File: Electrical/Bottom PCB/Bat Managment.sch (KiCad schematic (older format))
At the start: 6 parts

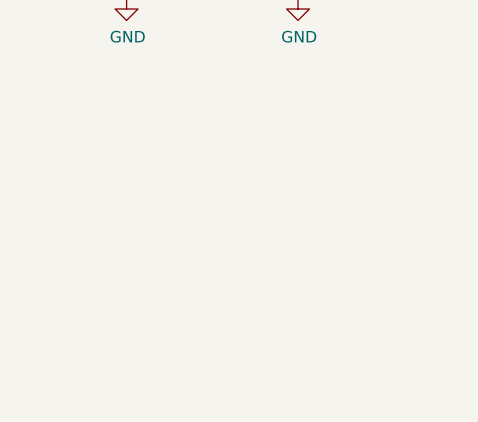
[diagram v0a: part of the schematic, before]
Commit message: removed the servos at the moment
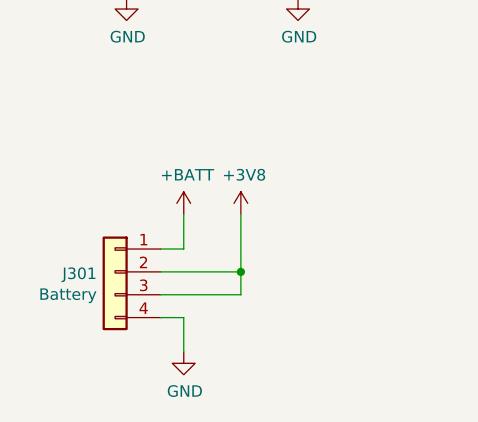
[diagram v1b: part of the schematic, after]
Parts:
- added J301: Battery, Connector_JST:JST_XH_B4B-XH-A_1x04_P2.50mm_Vertical, symbol Connector_Generic:Conn_01x04
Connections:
- net +3V8: now also J301.2 (Pin_2), J301.3 (Pin_3)
- net +BATT: now also J301.1 (Pin_1)
- net GND: now also J301.4 (Pin_4)
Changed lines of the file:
@@
 $Descr A4 11693 8268
 encoding utf-8
-Sheet 3 3
+Sheet 3 4
 Title ""
 Date ""
@@
 	1    0    0    -1
 $EndComp
+$Comp
+L Connector_Generic:Conn_01x04 J?
+U 1 1 5EBBDBE9
+P 1750 4400
+AR Path="/5EBBDBE9" Ref="J?"  Part="1"
+AR Path="/5ED67F7E/5EBBDBE9" Ref="J301"  Part="1"
+F 0 "J301" H 1830 4392 50  0000 L CNN
+F 1 "Battery" H 1830 4301 50  0000 L CNN
+F 2 "Connector_JST:JST_XH_B4B-XH-A_1x04_P2.50mm_Vertical" H 1750 4400 50  0001 C CNN
+F 3 "~" H 1750 4400 50  0001 C CNN
+	1    1750 4400
+	-1   0    0    -1
+$EndComp
+$Comp
+L power:+3V8 #PWR?
+U 1 1 5EBC1737
+P 2300 4150
+AR Path="/5EBB31C5/5EBC1737" Ref="#PWR?"  Part="1"
+AR Path="/5ED67F7E/5EBC1737" Ref="#PWR0308"  Part="1"
+F 0 "#PWR0308" H 2300 4000 50  0001 C CNN
+F 1 "+3V8" H 2315 4323 50  0000 C CNN
+F 2 "" H 2300 4150 50  0001 C CNN
+F 3 "" H 2300 4150 50  0001 C CNN
+	1    2300 4150
+	1    0    0    -1
+$EndComp
+$Comp
+L power:+BATT #PWR?
+U 1 1 5EBC1DA3
+P 2050 4150
+AR Path="/5EBC1DA3" Ref="#PWR?"  Part="1"
+AR Path="/5ED67F7E/5EBC1DA3" Ref="#PWR0307"  Part="1"
+F 0 "#PWR0307" H 2050 4000 50  0001 C CNN
+F 1 "+BATT" H 2065 4323 50  0000 C CNN
+F 2 "" H 2050 4150 50  0001 C CNN
+F 3 "" H 2050 4150 50  0001 C CNN
+	1    2050 4150
+	1    0    0    -1
+$EndComp
+$Comp
+L power:GND #PWR?
+U 1 1 5EBC24CC
+P 2050 4750
+AR Path="/5EBC24CC" Ref="#PWR?"  Part="1"
+AR Path="/5ED67F7E/5EBC24CC" Ref="#PWR0309"  Part="1"
+F 0 "#PWR0309" H 2050 4500 50  0001 C CNN
+F 1 "GND" H 2055 4577 50  0000 C CNN
+F 2 "" H 2050 4750 50  0001 C CNN
+F 3 "" H 2050 4750 50  0001 C CNN
+	1    2050 4750
+	1    0    0    -1
+$EndComp
+Wire Wire Line
+	2050 4150 2050 4300
+Wire Wire Line
+	2050 4300 1950 4300
+Wire Wire Line
+	1950 4400 2300 4400
+Wire Wire Line
+	1950 4500 2300 4500
+Wire Wire Line
+	2300 4150 2300 4400
+Connection ~ 2300 4400
+Wire Wire Line
+	2300 4400 2300 4500
+Wire Wire Line
+	1950 4600 2050 4600
+Wire Wire Line
+	2050 4600 2050 4750
 $EndSCHEMATC

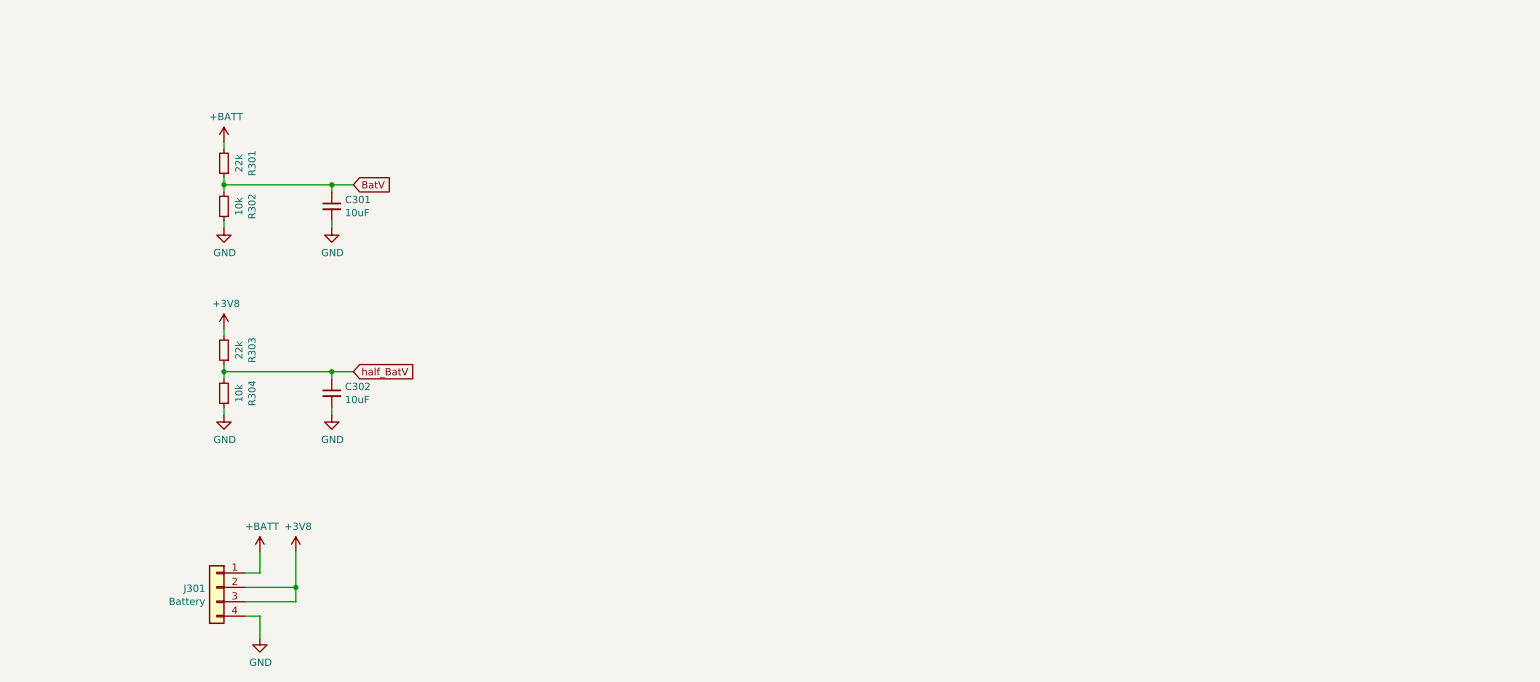
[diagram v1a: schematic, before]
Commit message: Added power switch
Some more modifications
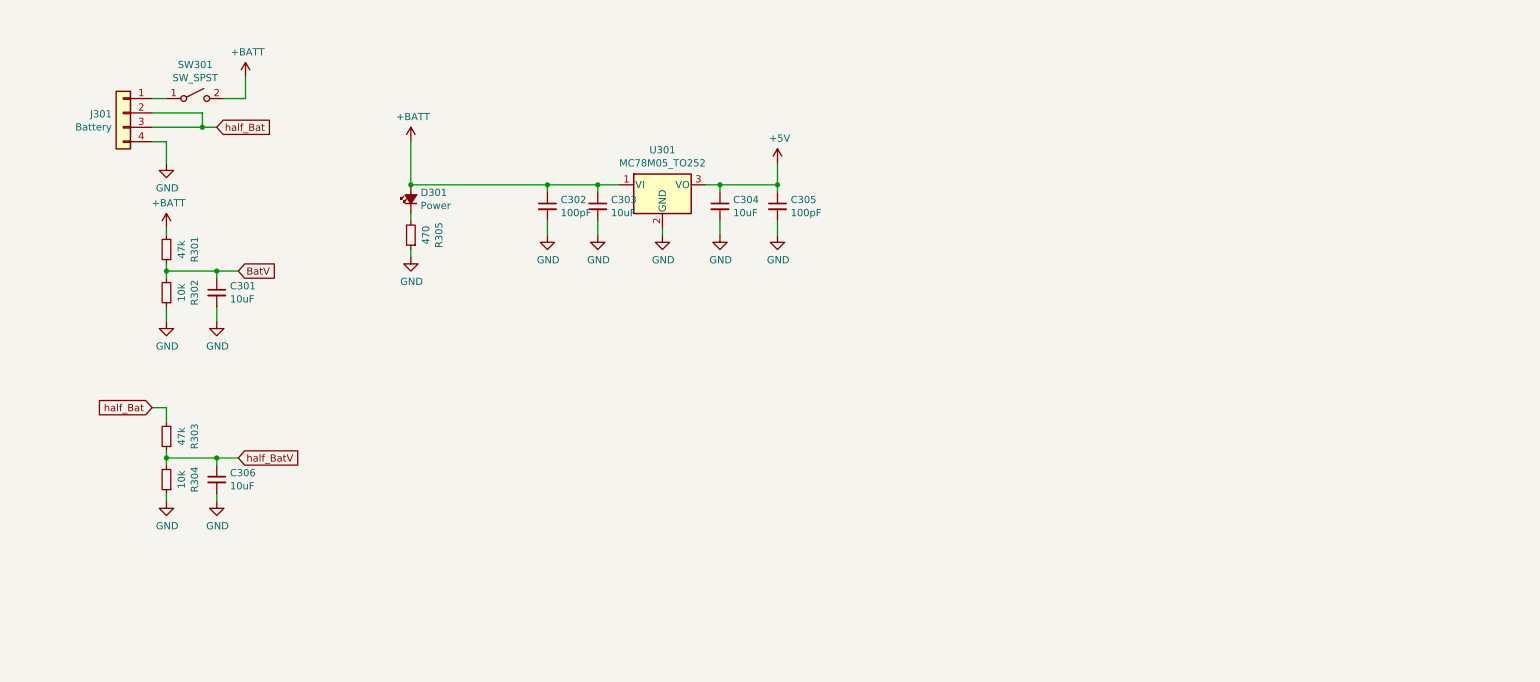
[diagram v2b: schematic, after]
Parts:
- added C302, C305: 100pF, Capacitor_SMD:C_1206_3216Metric_Pad1.42x1.75mm_HandSolder, symbol Device:C_Small
- added C303, C304: 10uF, Capacitor_SMD:C_1206_3216Metric_Pad1.42x1.75mm_HandSolder, symbol Device:C_Small
- added D301: Power, LED_SMD:LED_0805_2012Metric_Pad1.15x1.40mm_HandSolder, symbol Device:LED_Small_ALT
- added R305: 470, Resistor_SMD:R_1206_3216Metric_Pad1.42x1.75mm_HandSolder, symbol Device:R_Small
- added SW301: SW_SPST, Button_Switch_SMD:SW_SPST_B3U-3100P-B, symbol Switch:SW_SPST
- added U301: MC78M05_TO252, Package_TO_SOT_SMD:TO-252-2, symbol Regulator_Linear:MC78M05_TO252
- R301, R303: value 22k -> 47k
- renumbered C302 to C306
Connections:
- net +BATT: now also C302.1, C303.1, D301.2 (A), SW301.2 (B), U301.1 (VI); no longer J301.1 (Pin_1)
- net GND: now also C302.2, C303.2, C304.2, C305.2, R305.1, U301.2 (GND)
- net +3V8 renamed half_Bat
- new net: J301.1 (Pin_1), SW301.1 (A)
- new net: D301.1 (K), R305.2
- new net +5V: C304.1, C305.1, U301.3 (VO)
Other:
- moved on the sheet: C301, C306, J301, R301, R302, R303, R304

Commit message: added more stuff
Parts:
- renumbered C302 to C301, C303 to C302, C304 to C303, C305 to C304, C301 to C305, R303 to R302, R302 to R303
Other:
- moved on the sheet: C301, C302, C303, C304, C305, C306, D301, J301, R301, R302, R303, R304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

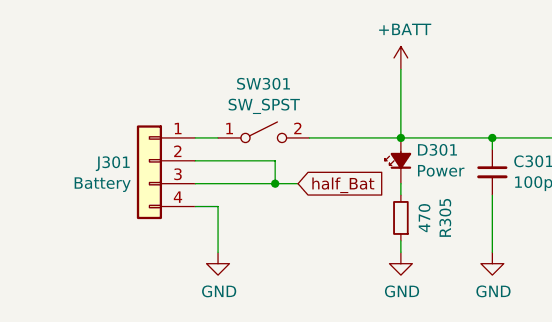
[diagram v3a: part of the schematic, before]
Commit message: changed from 1206 to 0805
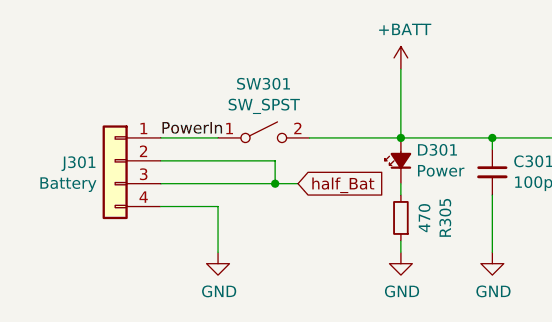
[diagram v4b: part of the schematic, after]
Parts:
- C301, C302, C303, C304, C305, C306: footprint Capacitor_SMD:C_1206_3216Metric_Pad1.42x1.75mm_HandSolder -> Capacitor_SMD:C_0805_2012Metric_Pad1.15x1.40mm_HandSolder
- R301, R302, R303, R304, R305: footprint Resistor_SMD:R_1206_3216Metric_Pad1.42x1.75mm_HandSolder -> Resistor_SMD:R_0805_2012Metric_Pad1.15x1.40mm_HandSolder
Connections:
- net PowerIn: now reaches J301.1 (Pin_1), SW301.1 (A)
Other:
- moved on the sheet: J301
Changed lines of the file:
@@
 F 0 "R303" V 5004 1100 50  0000 C CNN
 F 1 "10k" V 5095 1100 50  0000 C CNN
-F 2 "Resistor_SMD:R_1206_3216Metric_Pad1.42x1.75mm_HandSolder" H 5200 1100 50  0001 C CNN
+F 2 "Resistor_SMD:R_0805_2012Metric_Pad1.15x1.40mm_HandSolder" H 5200 1100 50  0001 C CNN
 F 3 "~" H 5200 1100 50  0001 C CNN
 	1    5200 1100
@@
 F 0 "R301" V 5004 800 50  0000 C CNN
 F 1 "47k" V 5095 800 50  0000 C CNN
-F 2 "Resistor_SMD:R_1206_3216Metric_Pad1.42x1.75mm_HandSolder" H 5200 800 50  0001 C CNN
+F 2 "Resistor_SMD:R_0805_2012Metric_Pad1.15x1.40mm_HandSolder" H 5200 800 50  0001 C CNN
 F 3 "~" H 5200 800 50  0001 C CNN
 	1    5200 800
@@
 F 0 "R304" V 6204 1100 50  0000 C CNN
 F 1 "10k" V 6295 1100 50  0000 C CNN
-F 2 "Resistor_SMD:R_1206_3216Metric_Pad1.42x1.75mm_HandSolder" H 6400 1100 50  0001 C CNN
+F 2 "Resistor_SMD:R_0805_2012Metric_Pad1.15x1.40mm_HandSolder" H 6400 1100 50  0001 C CNN
 F 3 "~" H 6400 1100 50  0001 C CNN
 	1    6400 1100
@@
 F 0 "R302" V 6204 800 50  0000 C CNN
 F 1 "47k" V 6295 800 50  0000 C CNN
-F 2 "Resistor_SMD:R_1206_3216Metric_Pad1.42x1.75mm_HandSolder" H 6400 800 50  0001 C CNN
+F 2 "Resistor_SMD:R_0805_2012Metric_Pad1.15x1.40mm_HandSolder" H 6400 800 50  0001 C CNN
 F 3 "~" H 6400 800 50  0001 C CNN
 	1    6400 800
@@
 F 0 "C306" H 6842 1146 50  0000 L CNN
 F 1 "10uF" H 6842 1055 50  0000 L CNN
-F 2 "Capacitor_SMD:C_1206_3216Metric_Pad1.42x1.75mm_HandSolder" H 6750 1100 50  0001 C CNN
+F 2 "Capacitor_SMD:C_0805_2012Metric_Pad1.15x1.40mm_HandSolder" H 6750 1100 50  0001 C CNN
 F 3 "~" H 6750 1100 50  0001 C CNN
 	1    6750 1100
@@
 L Connector_Generic:Conn_01x04 J?
 U 1 1 5EBBDBE9
-P 1400 1050
+P 1250 1050
 AR Path="/5EBBDBE9" Ref="J?"  Part="1"
 AR Path="/5ED67F7E/5EBBDBE9" Ref="J301"  Part="1"
-F 0 "J301" H 1480 1042 50  0000 L CNN
-F 1 "Battery" H 1480 951 50  0000 L CNN
-F 2 "Connector_JST:JST_XH_B4B-XH-A_1x04_P2.50mm_Vertical" H 1400 1050 50  0001 C CNN
-F 3 "~" H 1400 1050 50  0001 C CNN
-	1    1400 1050
+F 0 "J301" H 1330 1042 50  0000 L CNN
+F 1 "Battery" H 1330 951 50  0000 L CNN
+F 2 "Connector_JST:JST_XH_B4B-XH-A_1x04_P2.50mm_Vertical" H 1250 1050 50  0001 C CNN
+F 3 "~" H 1250 1050 50  0001 C CNN
+	1    1250 1050
 	-1   0    0    -1
 $EndComp
@@
 $EndComp
 Wire Wire Line
-	1600 950  1700 950
-Wire Wire Line
-	1600 1050 1950 1050
-Wire Wire Line
-	1600 1150 1950 1150
+	1450 950  1700 950
+Wire Wire Line
+	1450 1050 1950 1050
+Wire Wire Line
+	1450 1150 1950 1150
 Wire Wire Line
 	1950 1050 1950 1150
 Wire Wire Line
-	1600 1250 1700 1250
+	1450 1250 1700 1250
 Wire Wire Line
 	1700 1250 1700 1450
@@
 F 0 "C302" H 3392 1146 50  0000 L CNN
 F 1 "10uF" H 3392 1055 50  0000 L CNN
-F 2 "Capacitor_SMD:C_1206_3216Metric_Pad1.42x1.75mm_HandSolder" H 3300 1100 50  0001 C CNN
+F 2 "Capacitor_SMD:C_0805_2012Metric_Pad1.15x1.40mm_HandSolder" H 3300 1100 50  0001 C CNN
 F 3 "~" H 3300 1100 50  0001 C CNN
 	1    3300 1100
@@
 F 0 "C301" H 2992 1146 50  0000 L CNN
 F 1 "100pF" H 2992 1055 50  0000 L CNN
-F 2 "Capacitor_SMD:C_1206_3216Metric_Pad1.42x1.75mm_HandSolder" H 2900 1100 50  0001 C CNN
+F 2 "Capacitor_SMD:C_0805_2012Metric_Pad1.15x1.40mm_HandSolder" H 2900 1100 50  0001 C CNN
 F 3 "~" H 2900 1100 50  0001 C CNN
 	1    2900 1100
@@
 F 0 "C303" H 4292 1146 50  0000 L CNN
 F 1 "10uF" H 4292 1055 50  0000 L CNN
-F 2 "Capacitor_SMD:C_1206_3216Metric_Pad1.42x1.75mm_HandSolder" H 4200 1100 50  0001 C CNN
+F 2 "Capacitor_SMD:C_0805_2012Metric_Pad1.15x1.40mm_HandSolder" H 4200 1100 50  0001 C CNN
 F 3 "~" H 4200 1100 50  0001 C CNN
 	1    4200 1100
@@
 F 0 "C304" H 4692 1146 50  0000 L CNN
 F 1 "100pF" H 4692 1055 50  0000 L CNN
-F 2 "Capacitor_SMD:C_1206_3216Metric_Pad1.42x1.75mm_HandSolder" H 4600 1100 50  0001 C CNN
+F 2 "Capacitor_SMD:C_0805_2012Metric_Pad1.15x1.40mm_HandSolder" H 4600 1100 50  0001 C CNN
 F 3 "~" H 4600 1100 50  0001 C CNN
 	1    4600 1100
@@
 F 0 "C305" H 5642 1146 50  0000 L CNN
 F 1 "10uF" H 5642 1055 50  0000 L CNN
-F 2 "Capacitor_SMD:C_1206_3216Metric_Pad1.42x1.75mm_HandSolder" H 5550 1100 50  0001 C CNN
+F 2 "Capacitor_SMD:C_0805_2012Metric_Pad1.15x1.40mm_HandSolder" H 5550 1100 50  0001 C CNN
 F 3 "~" H 5550 1100 50  0001 C CNN
 	1    5550 1100
@@
 F 0 "R305" V 2304 1300 50  0000 C CNN
 F 1 "470" V 2395 1300 50  0000 C CNN
-F 2 "Resistor_SMD:R_1206_3216Metric_Pad1.42x1.75mm_HandSolder" H 2500 1300 50  0001 C CNN
+F 2 "Resistor_SMD:R_0805_2012Metric_Pad1.15x1.40mm_HandSolder" H 2500 1300 50  0001 C CNN
 F 3 "~" H 2500 1300 50  0001 C CNN
 	1    2500 1300
@@
 Wire Wire Line
 	2100 950  2500 950
+Text Label 1450 950  0    50   ~ 0
+PowerIn
 $EndSCHEMATC

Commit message: hello
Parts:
- removed C306: 10uF, Capacitor_SMD:C_0805_2012Metric_Pad1.15x1.40mm_HandSolder, symbol Device:C_Small
- removed R304: 10k, Resistor_SMD:R_0805_2012Metric_Pad1.15x1.40mm_HandSolder, symbol Device:R_Small
- removed U301: MC78M05_TO252, Package_TO_SOT_SMD:TO-252-2, symbol Regulator_Linear:MC78M05_TO252
- added C306, C308: 1uF, Capacitor_SMD:C_0603_1608Metric_Pad1.05x0.95mm_HandSolder, symbol Device:C
- added C307: 10uF, Capacitor_SMD:C_1206_3216Metric_Pad1.42x1.75mm_HandSolder, symbol Device:C
- added C309: 0.1uF, Capacitor_SMD:C_0603_1608Metric_Pad1.05x0.95mm_HandSolder, symbol Device:C
- added C310: 10uF, Capacitor_SMD:C_0805_2012Metric_Pad1.15x1.40mm_HandSolder, symbol Device:C
- added C311: 10uF, Capacitor_SMD:C_0805_2012Metric_Pad1.15x1.40mm_HandSolder, symbol Device:C_Small
- added D301, D303, D304, D307, D308, D309, D310, D311: SS24, Diode_SMD:D_SMB-SMC_Universal_Handsoldering, symbol Device:D_Schottky_Small_ALT
- added D305: Charging, LED_SMD:LED_0805_2012Metric_Pad1.15x1.40mm_HandSolder, symbol Device:LED_Small_ALT
- added D306: Standby, LED_SMD:LED_0805_2012Metric_Pad1.15x1.40mm_HandSolder, symbol Device:LED_Small_ALT
- added H301: +VE, TestPoint:TestPoint_Pad_D2.0mm, symbol Connector_Generic:Conn_01x01
- added H302: -Ve, TestPoint:TestPoint_Pad_D2.0mm, symbol Connector_Generic:Conn_01x01
- added J302: Charging Header, symbol Connector_Generic:Conn_01x02
- added L301: 3.3uH, symbol Device:L_Core_Iron_Small
- added R305: 30k, Resistor_SMD:R_0603_1608Metric_Pad0.98x0.95mm_HandSolder, symbol Device:R_Small
- added R306: 10k, Resistor_SMD:R_0603_1608Metric_Pad0.98x0.95mm_HandSolder, symbol Device:R_Small
- added R307, R308: 2R, Resistor_SMD:R_0603_1608Metric_Pad0.98x0.95mm_HandSolder, symbol Device:R
- added R309, R310: 1k, Resistor_SMD:R_0603_1608Metric_Pad0.98x0.95mm_HandSolder, symbol Device:R_Small
- added R311: 1k2, Resistor_SMD:R_0603_1608Metric_Pad0.98x0.95mm_HandSolder, symbol Device:R
- added U301: FP6298, Package_SO:SOIC-8_3.9x4.9mm_P1.27mm, symbol FP6298:FP6298
- added U302: AP2112K-3.3, Package_TO_SOT_SMD:SOT-23-5, symbol Regulator_Linear:AP2112K-3.3
- added U303: TP4056, Package_SO:SOP-8-1EP_4.57x4.57mm_P1.27mm_EP4.57x4.45mm_ThermalVias, symbol TP4056:TP4056
- C301, C304: value 100pF -> 22uF
- C302, C303: value 10uF -> 22uF
- J301: value Battery -> Battery 1S2P
- R301, R303: footprint Resistor_SMD:R_0805_2012Metric_Pad1.15x1.40mm_HandSolder -> Resistor_SMD:R_0603_1608Metric_Pad0.98x0.95mm_HandSolder
- R302: value 47k -> 73k; footprint Resistor_SMD:R_0805_2012Metric_Pad1.15x1.40mm_HandSolder -> Resistor_SMD:R_0603_1608Metric_Pad0.98x0.95mm_HandSolder
- R304: renamed from R305; footprint Resistor_SMD:R_0805_2012Metric_Pad1.15x1.40mm_HandSolder -> Resistor_SMD:R_0603_1608Metric_Pad0.98x0.95mm_HandSolder
- renumbered D301 to D302
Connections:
- net +5V: now also R302.2, D301.1 (K), D303.1 (K)
- net +BATT: now also C306.1, D307.1 (K), D308.1 (K), L301.1, U301.3 (VCC), U301.4 (En), U302.1 (VIN), U302.3 (EN)
- net GND: now also J301.1 (Pin_1), J301.2 (Pin_2), C306.2, C307.2, C308.2, C309.2, C310.2, C311.2, H302.1 (Pin_1), J302.2 (Pin_2), R305.1, R306.1, R311.1, U301.1 (GND), U301.5 (GND), U302.2 (GND), U303.1 (TEMP), U303.3 (GND), U303.PAD; no longer J301.4 (Pin_4)
- net PowerIn: now also J301.3 (Pin_3), J301.4 (Pin_4), C311.1, D309.2 (A), D310.2 (A), U303.5 (BAT); no longer J301.1 (Pin_1), SW301.1 (A)
- net BatV renamed A0
- removed net half_Bat: J301.2 (Pin_2), J301.3 (Pin_3), R302.2
- net half_BatV: no longer names the net of R302.1
- net half_BatV: now also R306.2, U301.6 (FB)
- new net: D309.1 (K), D310.1 (K), SW301.1 (A)
- new net: R305.2, U301.3 (VCC)
- new net: D301.2 (A), D303.2 (A), L301.2, U301.8 (LX)
- new net: D305.1 (K), R309.2
- new net: D305.2 (A), D306.2 (A), R307.1, R308.1, U303.4 (VCC), U303.8 (CE)
- new net: R309.1, U303.7 (~CHRG)
- new net: C310.1, D304.1 (K), D311.1 (K), R307.2, R308.2
- new net: R311.2, U303.2 (PROG)
- new net: R310.2, U303.6 (~STDBY)
- new net: D306.1 (K), R310.1
- new net +3V3: C307.1, C308.1, C309.1, U302.5 (VOUT)
- new net Charge: D304.2 (A), D307.2 (A), D308.2 (A), D311.2 (A), H301.1 (Pin_1), J302.1 (Pin_1)
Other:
- moved on the sheet: C303, C304, C305, J301, R301, R303, SW301
